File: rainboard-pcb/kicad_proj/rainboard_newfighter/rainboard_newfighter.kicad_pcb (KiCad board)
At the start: 2 copper layers, 260 x 253.6 mm, 513 parts, among them J1 EJ508A, J10 Conn_01x02_Female, J11 Conn_01x02_Female, J12 Conn_01x02_Female, J13 Conn_01x02_Female, J14 Conn_01x02_Female, J15 SDS-50J, J16 Conn_01x02_Female, J17 PH2-06-UA, J18 Conn_01x03, J19 Conn_01x03, J2 SDS-50J, J20 PH2-06-UA, J21 PH2-06-UA, J3 USB_B, J4 Conn_01x02_Female, J5 Conn_01x02_Female, J6 Conn_01x02_Female, J7 Conn_01x02_Female, J8 Conn_01x02_Female, J9 Conn_01x02_Female, Q1 30V 10mOhm, Q2 DUAL 30V NMOS, Q3 DUAL 30V NMOS, SW1 SANWA-OBSF24, SW10 SANWA-OBSF24, SW11 SANWA-OBSF24, SW12 SANWA-OBSF24, SW13 SANWA-OBSF24, SW14 SANWA-OBSF24, SW15 SANWA-OBSF24, SW16 SANWA-OBSF24, SW17 SANWA-OBSF24, SW18 SANWA-OBSF24, SW19 SANWA-OBSF24, SW2 SANWA-OBSF24, SW20 SANWA-OBSF24, SW21 SANWA-OBSF24, SW22 SANWA-OBSF24, SW23 SANWA-OBSF24, SW24 SANWA-OBSF24, SW25 SANWA-OBSF24, SW26 SANWA-OBSF24, SW27 SANWA-OBSF24, SW28 SANWA-OBSF24, SW29 SANWA-OBSF24, SW3 SANWA-OBSF24, SW30 SANWA-OBSF24, SW31 SANWA-OBSF24, SW32 SANWA-OBSF24, SW33 SANWA-OBSF24, SW34 SANWA-OBSF24, SW35 SANWA-OBSF24, SW36 SANWA-OBSF24, SW37 SANWA-OBSF24, SW38 SANWA-OBSF24, SW39 SANWA-OBSF24, SW4 SANWA-OBSF24, SW40 SANWA-OBSF24, SW41 SANWA-OBSF24, SW42 SANWA-OBSF24, SW43 SANWA-OBSF24, SW44 SANWA-OBSF24, SW45 SANWA-OBSF24, SW46 SANWA-OBSF24, SW47 SANWA-OBSF24, SW48 SANWA-OBSF24, SW49 SANWA-OBSF24, SW5 SANWA-OBSF24, SW50 SANWA-OBSF24, SW51 SANWA-OBSF24, SW52 SANWA-OBSF24, SW53 SANWA-OBSF24, SW54 SANWA-OBSF24, SW55 SANWA-OBSF24, SW56 SANWA-OBSF24, SW57 SANWA-OBSF24, SW58 SANWA-OBSF24, SW59 SANWA-OBSF24, SW6 SANWA-OBSF24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

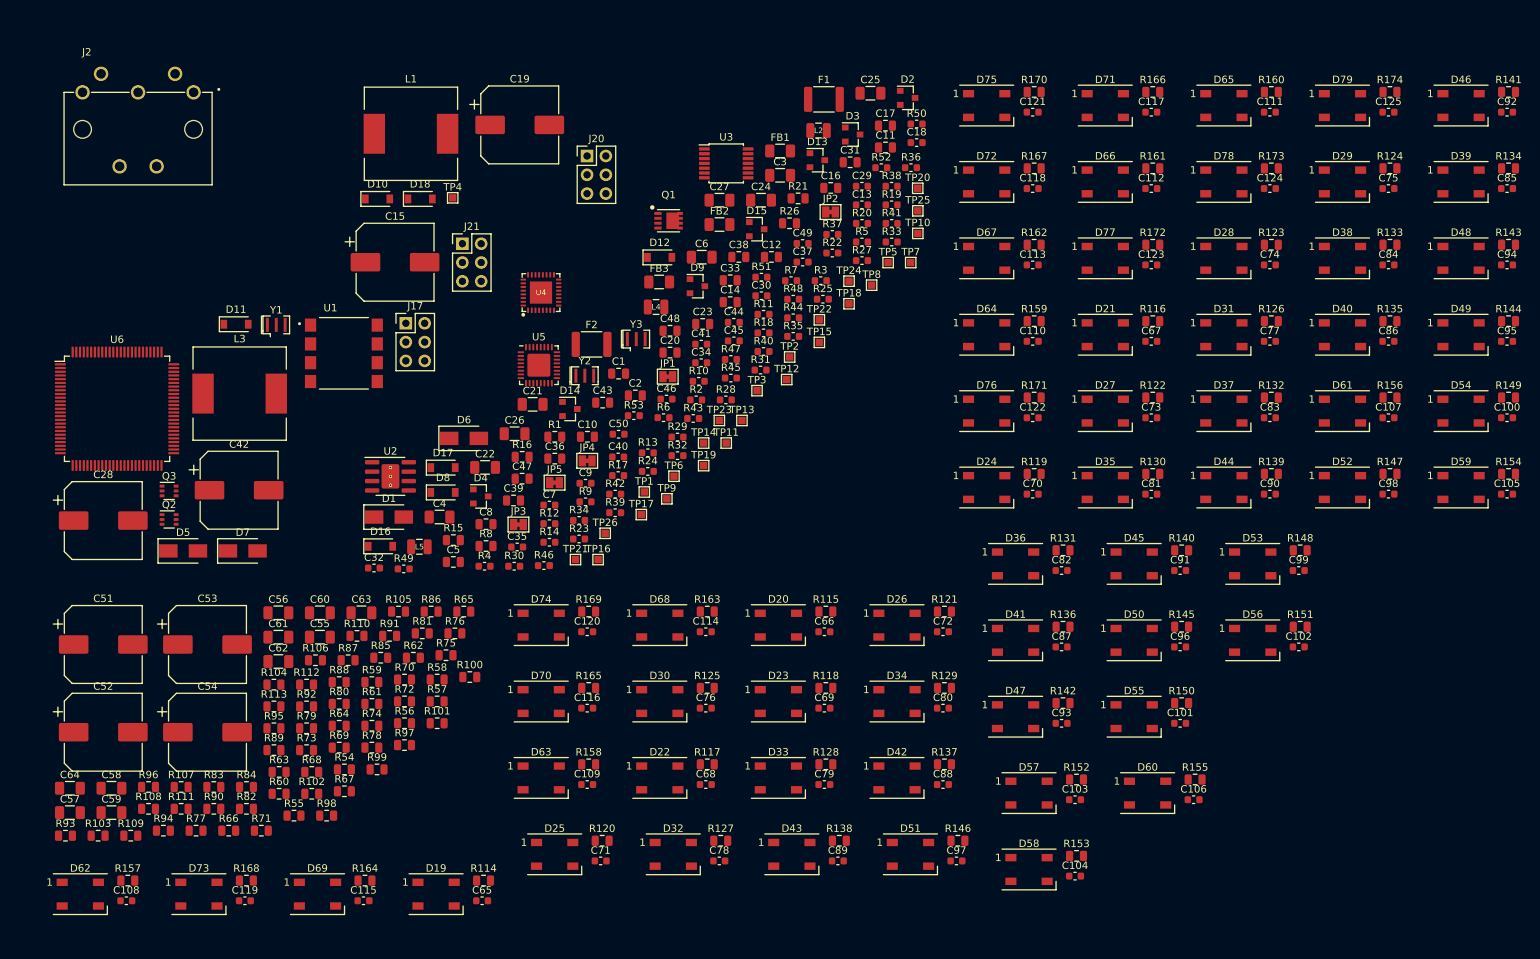
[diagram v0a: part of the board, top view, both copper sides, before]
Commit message: Swaps over to 5V  input supply
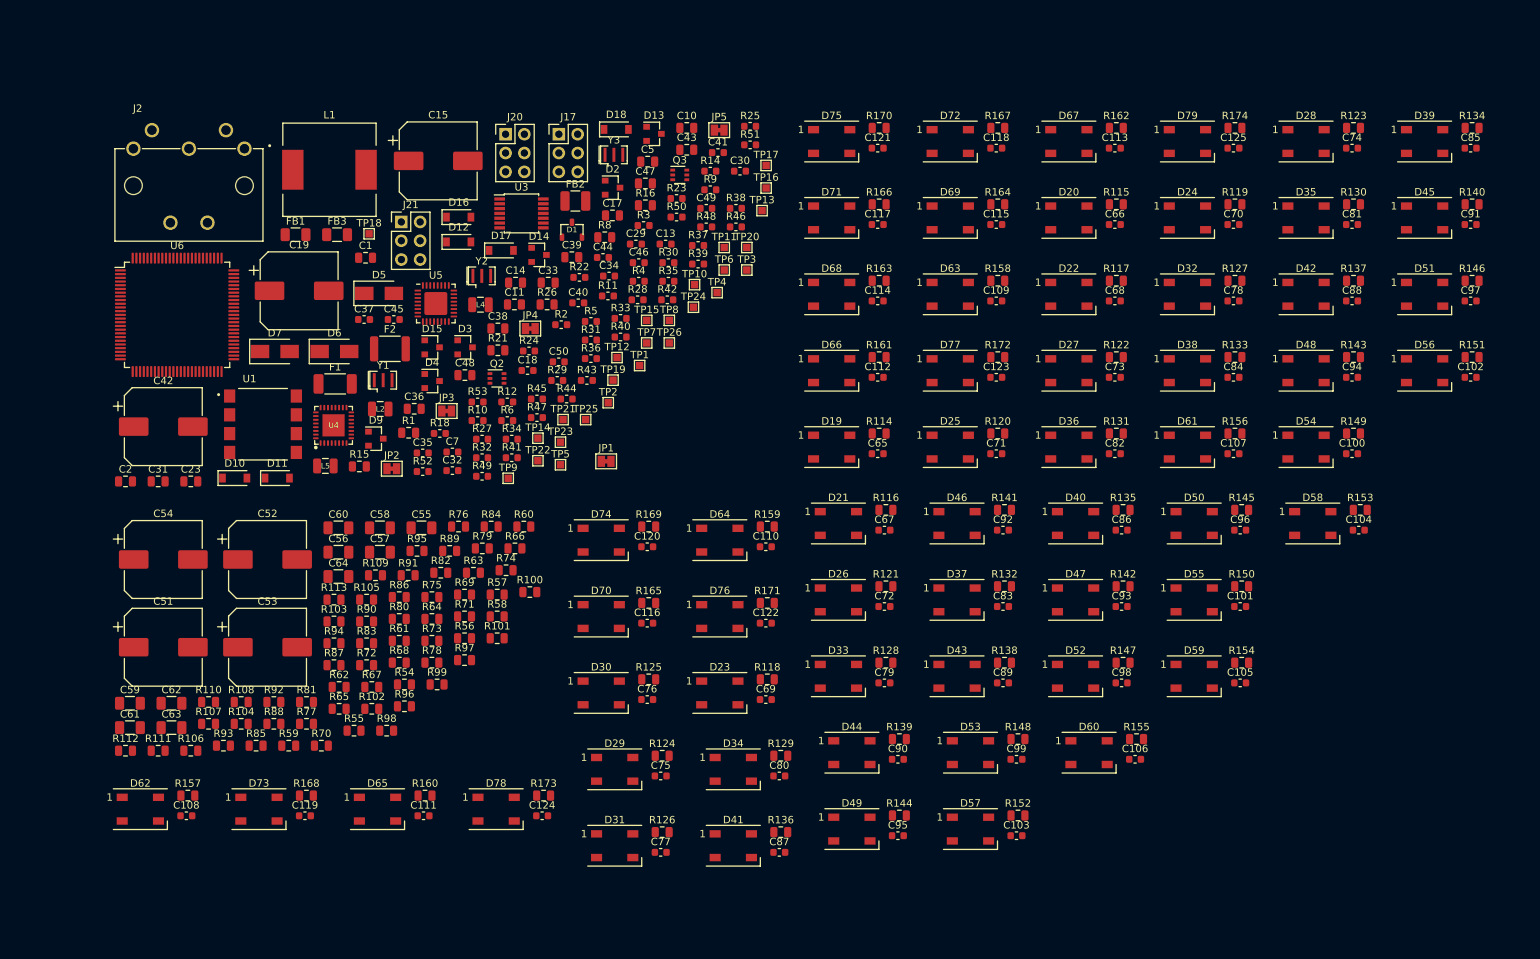
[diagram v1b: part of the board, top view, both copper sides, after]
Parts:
- removed C12, C16, C20, C8: 1uF 25V, Capacitor_SMD:C_0805_2012Metric
- removed C21, C22, C24, C25, C26, C27, C3, C4, C6: 10uF 25V, Capacitor_SMD:C_1206_3216Metric
- removed C28: 470uF 25V, Capacitor_SMD:CP_Elec_10x10
- removed C9: 100nf, Capacitor_SMD:C_0603_1608Metric
- removed D8: 40V 1A, Diode_SMD:D_SOD-123
- removed L3: 27uH, Inductor_SMD:L_12x12mm_H8mm
- removed Q1: 30V 10mOhm, rainboard_fp:PowerPAK_SO-8_Single
- removed R13, R17, R19, R7: 100k, Resistor_SMD:R_0603_1608Metric
- removed R20: 19.1k, Resistor_SMD:R_0603_1608Metric
- removed U2: RT8298, rainboard_fp:SOIC-8-1EP_3.9x4.9mm_P1.27mm_EP2.41x3.3mm_ThermalVias
- D1: value 12Vw -> 6V; footprint Diode_SMD:D_SMA -> rainboard_fp:SOT23-3
- F1: value 20V 3A -> 12V 5A; footprint Fuse:Fuse_1812_4532Metric -> Fuse:Fuse_2010_5025Metric
- FB2: value 4A Ferrite -> 10A Ferrite; footprint Inductor_SMD:L_1206_3216Metric -> Inductor_SMD:L_1210_3225Metric
- J1: value EJ508A -> 54-00167
- moved C111 148.7 mm to (210.3, 47.9)
- moved R160 148.7 mm to (210.5, 45.1)
- moved D65 148.7 mm to (204.1, 47.0)
- moved C124 129.8 mm to (226.3, 47.9)
- moved D78 129.8 mm to (220.1, 47.0)
- moved R173 129.8 mm to (226.6, 45.1)
- moved C75 126.3 mm to (242.4, 42.5)
- moved R124 126.3 mm to (242.6, 39.8)
- moved D29 126.3 mm to (236.2, 41.6)
- moved D69 125.1 mm to (281.5, -32.9)
- moved C115 125.1 mm to (287.7, -32.0)
- moved R164 125.1 mm to (287.9, -34.7)
- moved C77 107.4 mm to (242.4, 52.8)
- moved R126 107.4 mm to (242.6, 50.1)
- moved D31 107.4 mm to (236.2, 51.9)
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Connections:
- C13 pad 1: 12V_FILT -> 5V_WALL
- C15 pad 1: 12V_FILT -> 5V_WALL
- D1 pad 1: Net-(C5-Pad1) -> GND
- D6 pad 1: 12V_FILT -> 5V_WALL
- FB2 pad 1: 12V_FILT -> 5V_WALL
- JP1 pad 1: 5V_POW -> 5V_WALL
- L4 pad 2: 5V_POW -> 5V_WALL
- R14 pad 1: 12V_FILT -> 5V_WALL

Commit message: Modified electrolytics and setup board for layout
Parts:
- C15, C19, C42, C51, C52, C53, C54: value 470uF 25V -> 470uF 10V; footprint Capacitor_SMD:CP_Elec_10x10 -> Capacitor_SMD:CP_Elec_6.3x7.7
- D6: value 12Vw -> 6V; footprint Diode_SMD:D_SMA -> rainboard_fp:SOT23-3
- J1, J10, J11, J12, J13, J14, J15, J16, J18, J19, J3, J4, J5, J6, J7, J8, J9: moved to B.Cu
- moved D74 99.8 mm to (138.5, 38.5)
- moved D6 57.0 mm to (255.3, -14.8)
- moved J5 6.22 mm to (16.4, -123.4)
- moved J4 2.03 mm to (45.1, -121.3)
- moved J6 1.64 mm to (-18.7, -121.1)
- moved J7 1.64 mm to (-48.1, -121.1)
- moved J1 0.75 mm to (42.0, 130.7)
- turned J15 to 180 degrees
- turned J3 to 180 degrees
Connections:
- D6 pad 1: 5V_WALL -> GND
